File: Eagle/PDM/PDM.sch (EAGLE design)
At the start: 43 parts, among them U1 MIC29150/29300/29500VERTICAL, U2 MIC29150/29300/29500VERTICAL, U3 MIC29150/29300/29500VERTICAL

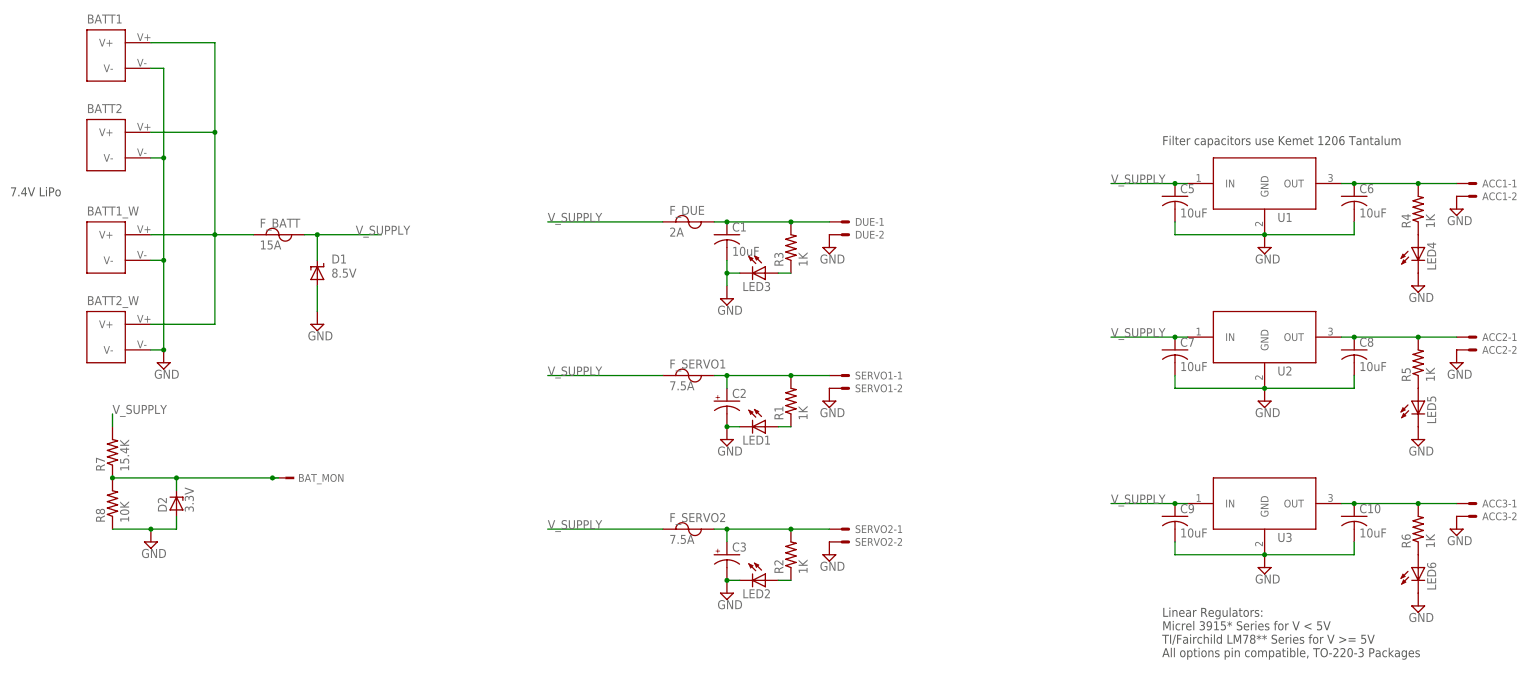
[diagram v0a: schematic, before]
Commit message: Removed Old PDM, Gerbers added, ready for BOM
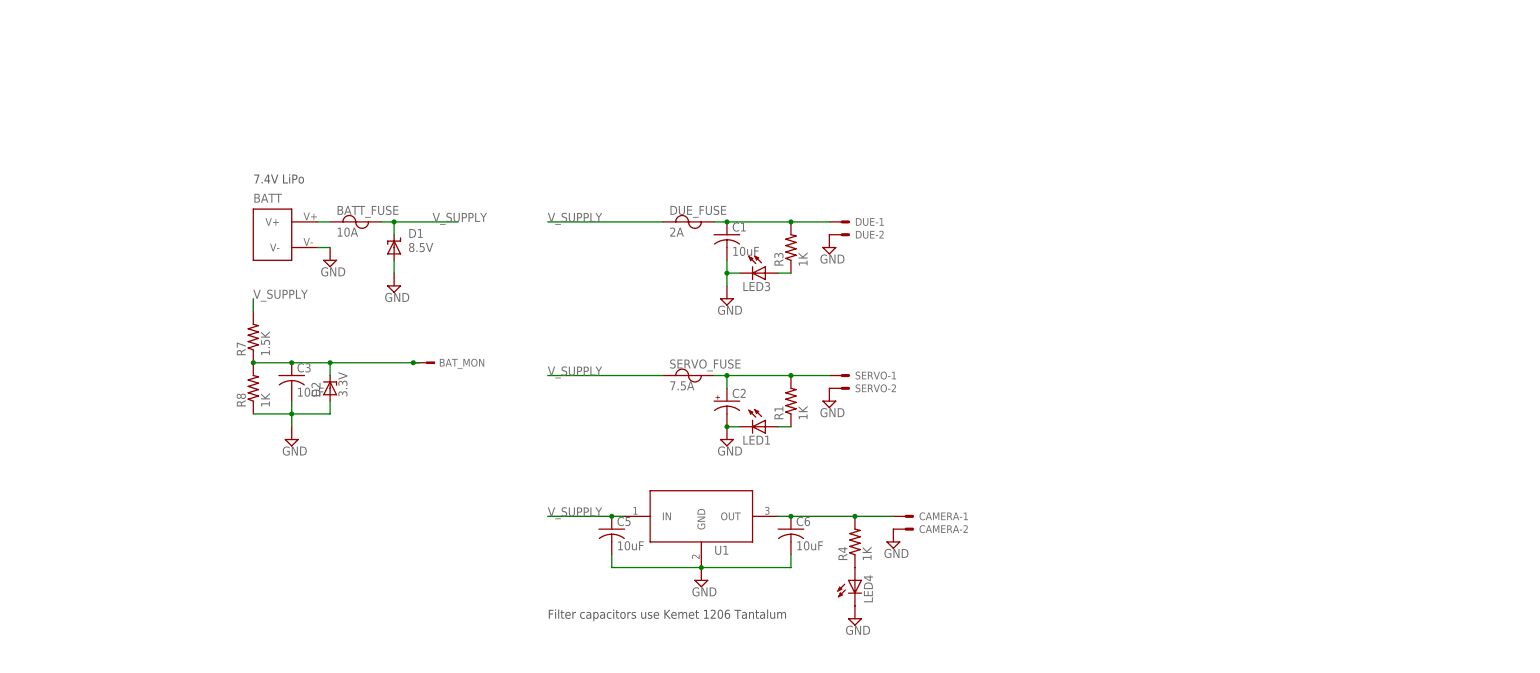
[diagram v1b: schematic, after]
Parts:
- removed ACC1, ACC2, ACC3, SERVO2: 5566-2, con-molex:5566-2
- removed BATT1, BATT2: CON_XT60-PCB_MOUNT, MRSDTeamB:CON_XT60-PCB_MOUNT
- removed BATT1_W, BATT2_W: CON_XT60-PIGTAIL, MRSDTeamB:CON_XT60-PIGTAIL
- removed C10, C7, C8, C9: 10uF, rcl:C-USC1206K
- removed F_BATT: 15A, MRSDTeamB:FUSE-ATO
- removed F_DUE: 2A, MRSDTeamB:FUSE-ATO
- removed F_SERVO1, F_SERVO2: 7.5A, MRSDTeamB:FUSE-ATO
- removed LED2, LED5, LED6: (no value), led:LEDSML1206
- removed R2, R5, R6: 1K, rcl:R-US_R1206
- removed U2, U3: MIC29150/29300/29500VERTICAL, MRSDTeamB:MIC29150/29300/29500VERTICAL
- added BATT: CON_XT60-, MRSDTeamB:CON_XT60-
- added BATT_FUSE: 10A, MRSDTeamB:FUSE-
- added CAMERA: 5566-2, con-molex:5566-2
- added DUE_FUSE: 2A, MRSDTeamB:FUSE-
- added SERVO_FUSE: 7.5A, MRSDTeamB:FUSE-
- C3: value (none) -> 10uF; device rcl:CPOL-USTT5D11 -> rcl:C-USC1206K
- D2: device diode:ZENER-DIODESMB -> diode:ZENER-DIODESOD80C
- R7: value 15.4K -> 1.5K
- R8: value 10K -> 1K
- renumbered SERVO1 to SERVO
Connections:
- removed net N$1: C3.+, F_SERVO2.2, R2.2, SERVO2-1.S
- removed net N$16: LED5.A, R5.1
- removed net N$19: ACC3-1.S, C10.1, R6.2, U3.OUT
- removed net N$22: LED6.A, R6.1
- removed net N$8: LED2.A, R2.1
- removed net N$9: ACC2-1.S, C8.1, R5.2, U2.OUT
- net GND: now also BATT.V-, C3.2, CAMERA-2.S; no longer ACC1-2.S, ACC2-2.S, ACC3-2.S, BATT1.V-, BATT1_W.V-, BATT2.V-, BATT2_W.V-, C10.2, C3.-, C7.2, C8.2, C9.2, LED2.C, LED5.C, LED6.C, SERVO2-2.S, U2.GND, U3.GND
- net N$15: now also SERVO_FUSE.2; no longer F_SERVO1.2
- net N$18: now also C3.1
- net N$2: now also BATT.V+, BATT_FUSE.1; no longer BATT1.V+, BATT1_W.V+, BATT2.V+, BATT2_W.V+, F_BATT.1
- net N$4: now also DUE_FUSE.2; no longer F_DUE.2
- net N$6: now also CAMERA-1.S; no longer ACC1-1.S
- net V_SUPPLY: now also BATT_FUSE.2, DUE_FUSE.1, SERVO_FUSE.1; no longer C7.1, C9.1, F_BATT.2, F_DUE.1, F_SERVO1.1, F_SERVO2.1, U2.IN, U3.IN
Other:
- note removed: "Linear Regulators: Micrel 3915* Series for V < 5V TI/Fairchild LM78** Series for V >= 5V All options pin compatible, TO-220-3 Packages"
- moved on the sheet: BAT_MON, C5, C6, D1, D2, LED4, R4, R7, R8, U1
